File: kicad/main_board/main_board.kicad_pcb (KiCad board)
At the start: 4 copper layers, 0 parts

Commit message: board outline
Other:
- board outline added: 198.1 x 61 mm

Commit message: layout front panel connectors
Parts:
- added C1: 330pF, Capacitor_SMD:C_0603_1608Metric, F.Cu at (-84.8, 68.6)
- added C10: 10uF, Capacitor_SMD:C_0805_2012Metric, F.Cu at (-69.3, 107.0)
- added C11: 1.8nF, Capacitor_SMD:C_0603_1608Metric, F.Cu at (-84.8, 88.7)
- added C12: 10uF, Capacitor_SMD:C_0805_2012Metric, F.Cu at (-69.3, 110.0)
- added C13: 680pF, Capacitor_SMD:C_0603_1608Metric, F.Cu at (-84.8, 91.2)
- added C14: 10uF, Capacitor_SMD:C_0805_2012Metric, F.Cu at (-69.3, 113.0)
- added C15: 15pF, Capacitor_SMD:C_0603_1608Metric, F.Cu at (-84.8, 93.7)
- added C16: 10uF, Capacitor_SMD:C_0805_2012Metric, F.Cu at (-69.3, 116.0)
- added C17: 33nF, Capacitor_SMD:C_0603_1608Metric, F.Cu at (-84.8, 96.2)
- added C18: 10uF, Capacitor_SMD:C_0805_2012Metric, F.Cu at (-69.3, 119.0)
- added C19: 10uF, Capacitor_SMD:C_0805_2012Metric, F.Cu at (-69.3, 122.1)
- added C2: 330pF, Capacitor_SMD:C_0603_1608Metric, F.Cu at (-84.8, 71.1)
- added C20: 33nF, Capacitor_SMD:C_0603_1608Metric, F.Cu at (-84.8, 98.7)
- added C21: 1uF, Capacitor_SMD:C_0603_1608Metric, F.Cu at (-84.8, 101.2)
- added C22: 10uF, Capacitor_SMD:C_0805_2012Metric, F.Cu at (-64.9, 104.0)
- added C23: 100nF, Capacitor_SMD:C_0603_1608Metric, F.Cu at (-80.8, 68.6)
- added C24: 1uF, Capacitor_SMD:C_0603_1608Metric, F.Cu at (-80.8, 71.1)
- added C25: 150pF, Capacitor_SMD:C_0603_1608Metric, F.Cu at (-80.8, 73.6)
- added C26: 47nF, Capacitor_SMD:C_0603_1608Metric, F.Cu at (-80.8, 76.1)
- added C27: 47nF, Capacitor_SMD:C_0603_1608Metric, F.Cu at (-80.8, 78.7)
- added C28: 150pF, Capacitor_SMD:C_0603_1608Metric, F.Cu at (-80.8, 81.2)
- added C29: 2.2uF, Capacitor_SMD:C_0603_1608Metric, F.Cu at (-80.8, 83.7)
- added C3: 10uF, Capacitor_SMD:C_0603_1608Metric, F.Cu at (-84.8, 73.6)
- added C30: 10uF, Capacitor_SMD:C_0805_2012Metric, F.Cu at (-64.9, 107.0)
- added C31: 100pF, Capacitor_SMD:C_0603_1608Metric, F.Cu at (-80.8, 86.2)
- added C32: 10uF, Capacitor_SMD:C_0805_2012Metric, F.Cu at (-64.9, 110.0)
- added C33: 1uF, Capacitor_SMD:C_0603_1608Metric, F.Cu at (-80.8, 88.7)
- added C34: 10uF, Capacitor_SMD:C_0805_2012Metric, F.Cu at (-64.9, 113.0)
- added C35: 10uF, Capacitor_SMD:C_0805_2012Metric, F.Cu at (-64.9, 116.0)
- added C36: 100nF, Capacitor_SMD:C_0603_1608Metric, F.Cu at (-80.8, 91.2)
- added C37: 10uF, Capacitor_SMD:C_0805_2012Metric, F.Cu at (-64.9, 119.0)
- added C38: 10uF, Capacitor_SMD:C_0805_2012Metric, F.Cu at (-64.9, 122.1)
- added C39: 10uF, Capacitor_SMD:C_0805_2012Metric, F.Cu at (-60.4, 104.0)
- added C4: 1uF, Capacitor_SMD:C_0603_1608Metric, F.Cu at (-84.8, 76.1)
- added C40: 10uF, Capacitor_SMD:C_0805_2012Metric, F.Cu at (-60.4, 107.0)
- added C41: 10uF, Capacitor_SMD:C_0805_2012Metric, F.Cu at (-60.4, 110.0)
- added C42: 100nF, Capacitor_SMD:C_0603_1608Metric, F.Cu at (-80.8, 93.7)
- added C43: 10uF, Capacitor_SMD:C_0805_2012Metric, F.Cu at (-60.4, 113.0)
- added C44: 10uF, Capacitor_SMD:C_0805_2012Metric, F.Cu at (-60.4, 116.0)
- added C45: 100nF, Capacitor_SMD:C_0603_1608Metric, F.Cu at (-80.8, 96.2)
- added C46: 100nF, Capacitor_SMD:C_0603_1608Metric, F.Cu at (-80.8, 98.7)
- added C47: 100nF, Capacitor_SMD:C_0603_1608Metric, F.Cu at (-80.8, 101.2)
- added C48: 100nF, Capacitor_SMD:C_0603_1608Metric, F.Cu at (-76.8, 68.6)
- added C49: 22uF, Capacitor_SMD:C_0805_2012Metric, F.Cu at (-60.4, 119.0)
- added C5: 100nF, Capacitor_SMD:C_0603_1608Metric, F.Cu at (-84.8, 78.7)
- added C50: 22uF, Capacitor_SMD:C_0805_2012Metric, F.Cu at (-60.4, 122.1)
- added C51: 10uF, Capacitor_SMD:C_0603_1608Metric, F.Cu at (-76.8, 71.1)
- added C52: 100nF, Capacitor_SMD:C_0603_1608Metric, F.Cu at (-76.8, 73.6)
- added C53: 1uF, Capacitor_SMD:C_0603_1608Metric, F.Cu at (-76.8, 76.1)
- added C54: 100nF, Capacitor_SMD:C_0402_1005Metric, F.Cu at (-51.6, 103.5)
- added C55: 100nF, Capacitor_SMD:C_0402_1005Metric, F.Cu at (-51.6, 105.5)
- added C56: 100nF, Capacitor_SMD:C_0402_1005Metric, F.Cu at (-51.6, 107.4)
- added C57: 100nF, Capacitor_SMD:C_0402_1005Metric, F.Cu at (-51.6, 109.4)
- added C58: 100nF, Capacitor_SMD:C_0402_1005Metric, F.Cu at (-51.6, 111.4)
- added C59: 100nF, Capacitor_SMD:C_0402_1005Metric, F.Cu at (-51.6, 113.3)
- added C6: 10uF, Capacitor_SMD:C_0603_1608Metric, F.Cu at (-84.8, 81.2)
- added C60: 100nF, Capacitor_SMD:C_0402_1005Metric, F.Cu at (-51.6, 115.3)
- added C61: 100nF, Capacitor_SMD:C_0402_1005Metric, F.Cu at (-51.6, 117.3)
- added C62: 10uF, Capacitor_SMD:C_0603_1608Metric, F.Cu at (-76.8, 78.7)
- added C63: 1uF, Capacitor_SMD:C_0603_1608Metric, F.Cu at (-76.8, 81.2)
- added C64: 100nF, Capacitor_SMD:C_0603_1608Metric, F.Cu at (-76.8, 83.7)
- added C65: 15pF, Capacitor_SMD:C_0603_1608Metric, F.Cu at (-76.8, 86.2)
- added C66: 15pF, Capacitor_SMD:C_0603_1608Metric, F.Cu at (-76.8, 88.7)
- added C67: 100nF, Capacitor_SMD:C_0603_1608Metric, F.Cu at (-76.8, 91.2)
- added C68: 1uF, Capacitor_SMD:C_0603_1608Metric, F.Cu at (-76.8, 93.7)
- added C69: 1uF, Capacitor_SMD:C_0603_1608Metric, F.Cu at (-76.8, 96.2)
- added C7: 10uF, Capacitor_SMD:C_0805_2012Metric, F.Cu at (-69.3, 104.0)
- added C70: 100nF, Capacitor_SMD:C_0603_1608Metric, F.Cu at (-76.8, 98.7)
- added C71: 100nF, Capacitor_SMD:C_0603_1608Metric, F.Cu at (-76.8, 101.2)
- added C72: 1uF, Capacitor_SMD:C_0603_1608Metric, F.Cu at (-72.8, 68.6)
- added C73: 10uF, Capacitor_SMD:C_0603_1608Metric, F.Cu at (-72.8, 71.1)
- added C74: 10nF, Capacitor_SMD:C_0603_1608Metric, F.Cu at (-72.8, 73.6)
- added C75: 10nF, Capacitor_SMD:C_0603_1608Metric, F.Cu at (-72.8, 76.1)
- added C76: 10nF, Capacitor_SMD:C_0603_1608Metric, F.Cu at (-72.8, 78.7)
- added C77: 1uF, Capacitor_SMD:C_0603_1608Metric, F.Cu at (-72.8, 81.2)
- added C78: 100nF, Capacitor_SMD:C_0603_1608Metric, F.Cu at (-72.8, 83.7)
- added C79: 100nF, Capacitor_SMD:C_0603_1608Metric, F.Cu at (-72.8, 86.2)
- added C8: 33pF, Capacitor_SMD:C_0603_1608Metric, F.Cu at (-84.8, 83.7)
- added C80: 10uF, Capacitor_SMD:C_0603_1608Metric, F.Cu at (-72.8, 88.7)
- added C81: 1uF, Capacitor_SMD:C_0603_1608Metric, F.Cu at (-72.8, 91.2)
- added C82: 10uF, Capacitor_SMD:C_0603_1608Metric, F.Cu at (-72.8, 93.7)
- added C83: 10uF, Capacitor_SMD:C_0603_1608Metric, F.Cu at (-72.8, 96.2)
- added C84: 100nF, Capacitor_SMD:C_0603_1608Metric, F.Cu at (-72.8, 98.7)
- added C85: 1uF, Capacitor_SMD:C_0603_1608Metric, F.Cu at (-72.8, 101.2)
- added C9: 100pF, Capacitor_SMD:C_0603_1608Metric, F.Cu at (-84.8, 86.2)
- added D10: BAV99, Package_TO_SOT_SMD:SOT-23, F.Cu at (-44.3, 79.0)
- added D2: 3V3, Diode_SMD:D_SOD-323, F.Cu at (-40.3, 104.0)
- added D3: 30V, Diode_SMD:D_SOD-323, F.Cu at (-40.3, 106.9)
- added D4: 30V, Diode_SMD:D_SOD-323, F.Cu at (-40.3, 109.9)
- added D5: 30V, Diode_SMD:D_SOD-323, F.Cu at (-40.3, 112.8)
- added D6: 30V, Diode_SMD:D_SOD-323, F.Cu at (-40.3, 115.8)
- added D7: PWR, LED_SMD:LED_0603_1608Metric, F.Cu at (-39.8, 97.8)
- added D8: BAV99, Package_TO_SOT_SMD:SOT-23, F.Cu at (-44.3, 69.8)
- added D9: BAV99, Package_TO_SOT_SMD:SOT-23, F.Cu at (-44.3, 74.4)
- added FID1: Fiducial, Fiducial:Fiducial_1mm_Mask2mm, F.Cu at (-14.0, 36.1)
- added FID2: Fiducial, Fiducial:Fiducial_1mm_Mask2mm, F.Cu at (-14.0, 39.6)
- added FID3: Fiducial, Fiducial:Fiducial_1mm_Mask2mm, F.Cu at (-14.0, 43.2)
- added H1: MountingHole, MountingHole:MountingHole_2.2mm_M2, F.Cu at (53.3, 68.6)
- added H2: MountingHole, MountingHole:MountingHole_2.2mm_M2, F.Cu at (246.4, 68.6)
- added H3: MountingHole, MountingHole:MountingHole_2.2mm_M2, F.Cu at (246.4, 124.5)
- added H4: MountingHole, MountingHole:MountingHole_2.2mm_M2, F.Cu at (53.3, 124.5)
- added H5: MountingHole, MountingHole:MountingHole_2.2mm_M2, F.Cu at (-27.9, 39.4)
- added J1: USB_C, Connector_USB:USB_C_Receptacle_GCT_USB4105-xx-A_16P_TopMnt_Horizontal, F.Cu at (88.9, 124.6)
- added J10: LINE_ALT, Connector_PinHeader_2.54mm:PinHeader_1x04_P2.54mm_Vertical, F.Cu at (133.3, 111.8)
- added J11: LINE, SaawLib:PJ-3062-CO, F.Cu at (129.5, 127.0)
- added J12: DRV1, Connector_PinSocket_2.54mm:PinSocket_1x13_P2.54mm_Vertical, F.Cu at (-59.7, 148.6)
- added J13: DRV2, Connector_PinSocket_2.54mm:PinSocket_1x13_P2.54mm_Vertical, F.Cu at (-12.7, 146.1)
- added J14: CH_IN, Connector_PinSocket_2.54mm:PinSocket_1x13_P2.54mm_Vertical, F.Cu at (-51.6, 148.6)
- added J15: CH1, SaawLib:PJ-3062-CO, F.Cu at (182.9, 127.0)
- added J16: CH2, SaawLib:PJ-3062-CO, F.Cu at (200.7, 127.0)
- added J17: CH3, SaawLib:PJ-3062-CO, F.Cu at (218.4, 127.0)
- added J18: CH4, SaawLib:PJ-3062-CO, F.Cu at (236.2, 127.0)
- added J2: TRIG_A, SaawLib:PJ-3062-CO, F.Cu at (147.3, 127.0)
- added J3: TRIG_B, SaawLib:PJ-3062-CO, F.Cu at (162.6, 127.0)
- added J4: BAT, Connector_AMASS:AMASS_XT30UPB-M_1x02_P5.0mm_Vertical, F.Cu at (-22.9, 163.8)
- added J5: BAT_LINK, Connector_JST:JST_XH_B4B-XH-A_1x04_P2.50mm_Vertical, F.Cu at (-6.41, 159.3)
- added J6: FRONT_PANEL, Connector_JST:JST_XH_B8B-XH-A_1x08_P2.50mm_Vertical, F.Cu at (-45.8, 154.2)
- added J7: I2C, Connector_PinHeader_2.54mm:PinHeader_1x04_P2.54mm_Vertical, F.Cu at (-47.0, 168.8)
- added J8: SWD, Connector_PinHeader_2.54mm:PinHeader_1x03_P2.54mm_Vertical, F.Cu at (-31.8, 171.5)
- added J9: MIC, SaawLib:PJ-3062-CO, F.Cu at (114.3, 127.0)
- added JP1: BAT_4S, Jumper:SolderJumper-2_P1.3mm_Bridged_RoundedPad1.0x1.5mm, F.Cu at (-34.3, 94.4)
- added JP2: LED, Jumper:SolderJumper-2_P1.3mm_Bridged_RoundedPad1.0x1.5mm, F.Cu at (-34.3, 98.0)
- added JP3: BOOT, Connector_PinHeader_2.54mm:PinHeader_1x02_P2.54mm_Vertical, F.Cu at (-19.1, 174.0)
- added JP4: CT1, Connector_PinHeader_2.54mm:PinHeader_1x02_P2.54mm_Vertical, F.Cu at (191.8, 115.6)
- added JP5: CT2, Connector_PinHeader_2.54mm:PinHeader_1x02_P2.54mm_Vertical, F.Cu at (209.6, 115.6)
- added JP6: CT3, Connector_PinHeader_2.54mm:PinHeader_1x02_P2.54mm_Vertical, F.Cu at (227.3, 115.6)
- added JP7: CT4, Connector_PinHeader_2.54mm:PinHeader_1x02_P2.54mm_Vertical, F.Cu at (245.1, 115.6)
- added L1: 2.2uH, Inductor_SMD:L_Vishay_IHLP-2525, F.Cu at (-31.6, 88.7)
- added L2: 12uH, Inductor_SMD:L_Sunlord_SWPA6020S, F.Cu at (-46.3, 106.3)
- added L3: 12uH, Inductor_SMD:L_Sunlord_SWPA6020S, F.Cu at (-46.3, 114.0)
- added MK1: MIC, Sensor_Audio:CUI_CMC-4013-SMT, F.Cu at (-47.4, 120.5)
- added Q1: DMP3018SFV, Package_SON:Diodes_PowerDI3333-8, F.Cu at (-35.4, 118.8)
- added Q10: AO3401A, Package_TO_SOT_SMD:SOT-23, F.Cu at (-44.3, 92.9)
- added Q2: AO3400A, Package_TO_SOT_SMD:SOT-23, F.Cu at (-44.3, 83.6)
- added Q3: CSD17551Q3A, Package_SON:VSON-8_3.3x3.3mm_P0.65mm_NexFET, F.Cu at (-39.0, 69.9)
- added Q4: CSD17551Q3A, Package_SON:VSON-8_3.3x3.3mm_P0.65mm_NexFET, F.Cu at (-39.0, 74.8)
- added Q5: CSD17551Q3A, Package_SON:VSON-8_3.3x3.3mm_P0.65mm_NexFET, F.Cu at (-39.0, 79.8)
- added Q6: CSD17551Q3A, Package_SON:VSON-8_3.3x3.3mm_P0.65mm_NexFET, F.Cu at (-39.0, 84.7)
- added Q7: CSD25402Q3A, Package_SON:VSON-8_3.3x3.3mm_P0.65mm_NexFET, F.Cu at (-39.0, 89.7)
- added Q8: AO3400A, Package_TO_SOT_SMD:SOT-23, F.Cu at (-44.3, 88.3)
- added Q9: DMP3018SFV, Package_SON:Diodes_PowerDI3333-8, F.Cu at (-35.4, 123.7)
- added R1: 10k, Resistor_SMD:R_0603_1608Metric, F.Cu at (-68.8, 68.6)
- added R10: 100k, Resistor_SMD:R_0603_1608Metric, F.Cu at (-68.8, 91.2)
- added R11: 10k, Resistor_SMD:R_0603_1608Metric, F.Cu at (-68.8, 93.7)
- added R12: 22k, Resistor_SMD:R_0603_1608Metric, F.Cu at (-68.8, 96.2)
- added R13: 100, Resistor_SMD:R_1206_3216Metric, F.Cu at (-27.9, 104.1)
- added R14: 100k, Resistor_SMD:R_0603_1608Metric, F.Cu at (-68.8, 98.7)
- added R15: 22k, Resistor_SMD:R_0603_1608Metric, F.Cu at (-68.8, 101.2)
- added R16: 100k, Resistor_SMD:R_0603_1608Metric, F.Cu at (-64.8, 68.6)
- added R17: 2k, Resistor_SMD:R_1206_3216Metric, F.Cu at (-27.9, 107.4)
- added R18: 39k, Resistor_SMD:R_0603_1608Metric, F.Cu at (-64.8, 71.1)
- added R19: 300k, Resistor_SMD:R_0603_1608Metric, F.Cu at (-64.8, 73.6)
- added R2: 10k, Resistor_SMD:R_0603_1608Metric, F.Cu at (-68.8, 71.1)
- added R20: 220k, Resistor_SMD:R_0603_1608Metric, F.Cu at (-64.8, 76.1)
- added R21: 10k, Resistor_SMD:R_0603_1608Metric, F.Cu at (-64.8, 78.7)
- added R22: 4.99, Resistor_SMD:R_0603_1608Metric, F.Cu at (-64.8, 81.2)
- added R23: 0.01, Resistor_SMD:R_1206_3216Metric, F.Cu at (-27.9, 110.7)
- added R24: 10, Resistor_SMD:R_0603_1608Metric, F.Cu at (-64.8, 83.7)
- added R25: 4.99, Resistor_SMD:R_0603_1608Metric, F.Cu at (-64.8, 86.2)
- added R26: 10, Resistor_SMD:R_0603_1608Metric, F.Cu at (-64.8, 88.7)
- added R27: 10k, Resistor_SMD:R_0603_1608Metric, F.Cu at (-64.8, 91.2)
- added R28: 10k, Resistor_SMD:R_0603_1608Metric, F.Cu at (-64.8, 93.7)
- added R29: 27k, Resistor_SMD:R_0603_1608Metric, F.Cu at (-64.8, 96.2)
- added R3: 10k, Resistor_SMD:R_0603_1608Metric, F.Cu at (-68.8, 73.6)
- added R30: 10, Resistor_SMD:R_0603_1608Metric, F.Cu at (-64.8, 98.7)
- added R31: 0.01, Resistor_SMD:R_1206_3216Metric, F.Cu at (-27.9, 114.0)
- added R32: 10, Resistor_SMD:R_0603_1608Metric, F.Cu at (-64.8, 101.2)
- added R33: 39k, Resistor_SMD:R_0603_1608Metric, F.Cu at (-60.8, 68.6)
- added R34: 39k, Resistor_SMD:R_0603_1608Metric, F.Cu at (-60.8, 71.1)
- added R35: 100k, Resistor_SMD:R_0603_1608Metric, F.Cu at (-60.8, 73.6)
- added R36: 100k, Resistor_SMD:R_0603_1608Metric, F.Cu at (-60.8, 76.1)
- added R37: 1k, Resistor_SMD:R_0603_1608Metric, F.Cu at (-60.8, 78.7)
- added R38: 1M, Resistor_SMD:R_0603_1608Metric, F.Cu at (-60.8, 81.2)
- added R39: 100k, Resistor_SMD:R_0603_1608Metric, F.Cu at (-60.8, 83.7)
- added R4: 10k, Resistor_SMD:R_0603_1608Metric, F.Cu at (-68.8, 76.1)
- added R40: 2.2k, Resistor_SMD:R_0603_1608Metric, F.Cu at (-60.8, 86.2)
- added R41: 82k, Resistor_SMD:R_0603_1608Metric, F.Cu at (-60.8, 88.7)
- added R42: 22k, Resistor_SMD:R_0603_1608Metric, F.Cu at (-60.8, 91.2)
- added R43: 51k, Resistor_SMD:R_0603_1608Metric, F.Cu at (-60.8, 93.7)
- added R44: 22k, Resistor_SMD:R_0603_1608Metric, F.Cu at (-60.8, 96.2)
- added R45: 2.2k, Resistor_SMD:R_0603_1608Metric, F.Cu at (-60.8, 98.7)
- added R46: 10k, Resistor_SMD:R_0603_1608Metric, F.Cu at (-60.8, 101.2)
- added R47: 2.2k, Resistor_SMD:R_0603_1608Metric, F.Cu at (-56.7, 68.6)
- added R48: 27, Resistor_SMD:R_0603_1608Metric, F.Cu at (-56.7, 71.1)
- added R49: 27, Resistor_SMD:R_0603_1608Metric, F.Cu at (-56.7, 73.6)
- added R5: 100k, Resistor_SMD:R_0603_1608Metric, F.Cu at (-68.8, 78.7)
- added R50: 100k, Resistor_SMD:R_0603_1608Metric, F.Cu at (-56.7, 76.1)
- added R51: 2.2k, Resistor_SMD:R_0603_1608Metric, F.Cu at (-56.7, 78.7)
- added R52: 2.2k, Resistor_SMD:R_0603_1608Metric, F.Cu at (-56.7, 81.2)
- added R53: 100, Resistor_SMD:R_0603_1608Metric, F.Cu at (-56.7, 83.7)
- added R54: 1k, Resistor_SMD:R_0603_1608Metric, F.Cu at (-56.7, 86.2)
- added R55: 1k, Resistor_SMD:R_0603_1608Metric, F.Cu at (-56.7, 88.7)
- added R56: 10k, Resistor_SMD:R_0603_1608Metric, F.Cu at (-56.7, 91.2)
- added R57: 100k, Resistor_SMD:R_0603_1608Metric, F.Cu at (-56.7, 93.7)
- added R58: 100, Resistor_SMD:R_0603_1608Metric, F.Cu at (-56.7, 96.2)
- added R59: 2.2k, Resistor_SMD:R_0603_1608Metric, F.Cu at (-56.7, 98.7)
- added R6: 1k, Resistor_SMD:R_0603_1608Metric, F.Cu at (-68.8, 81.2)
- added R60: 100k, Resistor_SMD:R_0603_1608Metric, F.Cu at (-56.7, 101.2)
- added R61: 100k, Resistor_SMD:R_0603_1608Metric, F.Cu at (-52.7, 68.6)
- added R62: 1M, Resistor_SMD:R_0603_1608Metric, F.Cu at (-52.7, 71.1)
- added R63: 1k, Resistor_SMD:R_0603_1608Metric, F.Cu at (-52.7, 73.6)
- added R64: 2.2k, Resistor_SMD:R_0603_1608Metric, F.Cu at (-52.7, 76.1)
- added R65: 1k, Resistor_SMD:R_0603_1608Metric, F.Cu at (-52.7, 78.7)
- added R66: 1k, Resistor_SMD:R_0603_1608Metric, F.Cu at (-52.7, 81.2)
- added R67: 1k, Resistor_SMD:R_0603_1608Metric, F.Cu at (-52.7, 83.7)
- added R68: 1k, Resistor_SMD:R_0603_1608Metric, F.Cu at (-52.7, 86.2)
- added R69: 100k, Resistor_SMD:R_0603_1608Metric, F.Cu at (-52.7, 88.7)
- added R7: 1k, Resistor_SMD:R_0603_1608Metric, F.Cu at (-68.8, 83.7)
- added R70: 100k, Resistor_SMD:R_0603_1608Metric, F.Cu at (-52.7, 91.2)
- added R71: 10k, Resistor_SMD:R_0603_1608Metric, F.Cu at (-52.7, 93.7)
- added R72: 1M, Resistor_SMD:R_0603_1608Metric, F.Cu at (-52.7, 96.2)
- added R73: 1M, Resistor_SMD:R_0603_1608Metric, F.Cu at (-52.7, 98.7)
- added R74: 100k, Resistor_SMD:R_0603_1608Metric, F.Cu at (-52.7, 101.2)
- added R75: 100k, Resistor_SMD:R_0603_1608Metric, F.Cu at (-48.7, 68.6)
- added R76: 1k, Resistor_SMD:R_0603_1608Metric, F.Cu at (-48.7, 71.1)
- added R77: 1k, Resistor_SMD:R_0603_1608Metric, F.Cu at (-48.7, 73.6)
- added R78: 2.2k, Resistor_SMD:R_0603_1608Metric, F.Cu at (-48.7, 76.1)
- added R79: 2.2k, Resistor_SMD:R_0603_1608Metric, F.Cu at (-48.7, 78.7)
- added R8: 1k, Resistor_SMD:R_0603_1608Metric, F.Cu at (-68.8, 86.2)
- added R80: 10k, Resistor_SMD:R_0603_1608Metric, F.Cu at (-48.7, 81.2)
- added R81: 10k, Resistor_SMD:R_0603_1608Metric, F.Cu at (-48.7, 83.7)
- added R82: 1M, Resistor_SMD:R_0603_1608Metric, F.Cu at (-48.7, 86.2)
- added R83: 6.2k, Resistor_SMD:R_0603_1608Metric, F.Cu at (-48.7, 88.7)
- added R84: 82k, Resistor_SMD:R_0603_1608Metric, F.Cu at (-48.7, 91.2)
- added R85: 1.2k, Resistor_SMD:R_0603_1608Metric, F.Cu at (-48.7, 93.7)
- added R86: 100k, Resistor_SMD:R_0603_1608Metric, F.Cu at (-48.7, 96.2)
- added R87: 10k, Resistor_SMD:R_0603_1608Metric, F.Cu at (-48.7, 98.7)
- added R9: 1k, Resistor_SMD:R_0603_1608Metric, F.Cu at (-68.8, 88.7)
- added SW1: PWR, Button_Switch_THT:SW_Tactile_SPST_Angled_PTS645Vx31-2LFS, F.Cu at (65.8, 121.3)
- added TP1: GND, TestPoint:TestPoint_Pad_D1.0mm, F.Cu at (-85.3, 104.0)
- added TP10: CELL, TestPoint:TestPoint_Pad_D1.0mm, F.Cu at (-82.2, 110.1)
- added TP11: GND, TestPoint:TestPoint_Pad_D1.0mm, F.Cu at (-82.2, 113.2)
- added TP12: GND, TestPoint:TestPoint_Pad_D1.0mm, F.Cu at (-82.2, 116.2)
- added TP13: VIN, TestPoint:TestPoint_Pad_D1.0mm, F.Cu at (-82.2, 119.3)
- added TP14: GND, TestPoint:TestPoint_Pad_D1.0mm, F.Cu at (-82.2, 122.3)
- added TP15: GND, TestPoint:TestPoint_Pad_D1.0mm, F.Cu at (-79.2, 104.0)
- added TP16: GND, TestPoint:TestPoint_Pad_D1.0mm, F.Cu at (-79.2, 107.1)
- added TP17: GND, TestPoint:TestPoint_Pad_D1.0mm, F.Cu at (-79.2, 110.1)
- added TP18: VIN, TestPoint:TestPoint_Pad_D1.0mm, F.Cu at (-79.2, 113.2)
- added TP19: VIN, TestPoint:TestPoint_Pad_D1.0mm, F.Cu at (-79.2, 116.2)
- added TP2: GND, TestPoint:TestPoint_Pad_D1.0mm, F.Cu at (-85.3, 107.1)
- added TP20: 5V, TestPoint:TestPoint_Pad_D1.0mm, F.Cu at (-79.2, 119.3)
- added TP21: 3V3, TestPoint:TestPoint_Pad_D1.0mm, F.Cu at (-79.2, 122.3)
- added TP22: GND, TestPoint:TestPoint_Pad_D1.0mm, F.Cu at (-76.1, 104.0)
- added TP23: DSCL, TestPoint:TestPoint_Pad_D1.0mm, F.Cu at (-76.1, 107.1)
- added TP24: DSDA, TestPoint:TestPoint_Pad_D1.0mm, F.Cu at (-76.1, 110.1)
- added TP25: ~{LDAC}, TestPoint:TestPoint_Pad_D1.0mm, F.Cu at (-76.1, 113.2)
- added TP26: RDY, TestPoint:TestPoint_Pad_D1.0mm, F.Cu at (-76.1, 116.2)
- added TP27: GND, TestPoint:TestPoint_Pad_D1.0mm, F.Cu at (-76.1, 119.3)
- added TP28: RUN, TestPoint:TestPoint_Pad_D1.0mm, F.Cu at (-76.1, 122.3)
- added TP29: VREF, TestPoint:TestPoint_Pad_D1.0mm, F.Cu at (-73.1, 104.0)
- added TP3: SBU1, TestPoint:TestPoint_Pad_D1.0mm, F.Cu at (-85.3, 110.1)
- added TP30: GND, TestPoint:TestPoint_Pad_D1.0mm, F.Cu at (-73.1, 107.1)
- added TP31: MOP, TestPoint:TestPoint_Pad_D1.0mm, F.Cu at (-73.1, 110.1)
- added TP32: ROP, TestPoint:TestPoint_Pad_D1.0mm, F.Cu at (-73.1, 113.2)
- added TP33: TOP, TestPoint:TestPoint_Pad_D1.0mm, F.Cu at (-73.1, 116.2)
- added TP34: GND, TestPoint:TestPoint_Pad_D1.0mm, F.Cu at (-73.1, 119.3)
- added TP4: SBU2, TestPoint:TestPoint_Pad_D1.0mm, F.Cu at (-85.3, 113.2)
- added TP5: VBUS, TestPoint:TestPoint_Pad_D1.0mm, F.Cu at (-85.3, 116.2)
- added TP6: ILIM, TestPoint:TestPoint_Pad_D1.0mm, F.Cu at (-85.3, 119.3)
- added TP7: CHRG_OK, TestPoint:TestPoint_Pad_D1.0mm, F.Cu at (-85.3, 122.3)
- added TP8: ~{PROCHOT}, TestPoint:TestPoint_Pad_D1.0mm, F.Cu at (-82.2, 104.0)
- added TP9: VSYS, TestPoint:TestPoint_Pad_D1.0mm, F.Cu at (-82.2, 107.1)
- added U1: SRV05-4, Package_TO_SOT_SMD:SOT-23-6, F.Cu at (-55.6, 104.9)
- added U10: MCP4451-503, Package_SO:TSSOP-20_4.4x6.5mm_P0.65mm, F.Cu at (-31.8, 80.7)
- added U11: MCP6002, Package_SO:MSOP-8_3x3mm_P0.65mm, F.Cu at (-34.5, 109.4)
- added U12: MCP6002, Package_SO:MSOP-8_3x3mm_P0.65mm, F.Cu at (-34.5, 114.0)
- added U2: SRV05-4, Package_TO_SOT_SMD:SOT-23-6, F.Cu at (-55.6, 109.5)
- added U3: FUSB302B, Package_DFN_QFN:WQFN-14-1EP_2.5x2.5mm_P0.5mm_EP1.45x1.45mm, F.Cu at (-55.8, 123.4)
- added U4: BQ25703A, Package_DFN_QFN:Texas_S-PWQFN-N32_EP2.8x2.8mm_ThermalVias, F.Cu at (-29.0, 95.8)
- added U5: TPS560430, Package_TO_SOT_SMD:SOT-23-6, F.Cu at (-55.6, 114.1)
- added U6: TPS560430, Package_TO_SOT_SMD:SOT-23-6, F.Cu at (-55.6, 118.8)
- added U7: MCP4728, Package_SO:MSOP-10_3x3mm_P0.5mm, F.Cu at (-34.5, 104.8)
- added U8: RP2040, Package_DFN_QFN:QFN-56-1EP_7x7mm_P0.4mm_EP3.2x3.2mm, F.Cu at (-31.9, 72.0)
- added U9: W25Q128JVP, Package_SON:WSON-8-1EP_6x5mm_P1.27mm_EP3.4x4.3mm, F.Cu at (-28.5, 119.6)
- added Y1: 12MHz, Crystal:Crystal_SMD_3225-4Pin_3.2x2.5mm, F.Cu at (-39.2, 94.3)
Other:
- board text added: "Button Cap"
- board text added: "Front Panel ->"

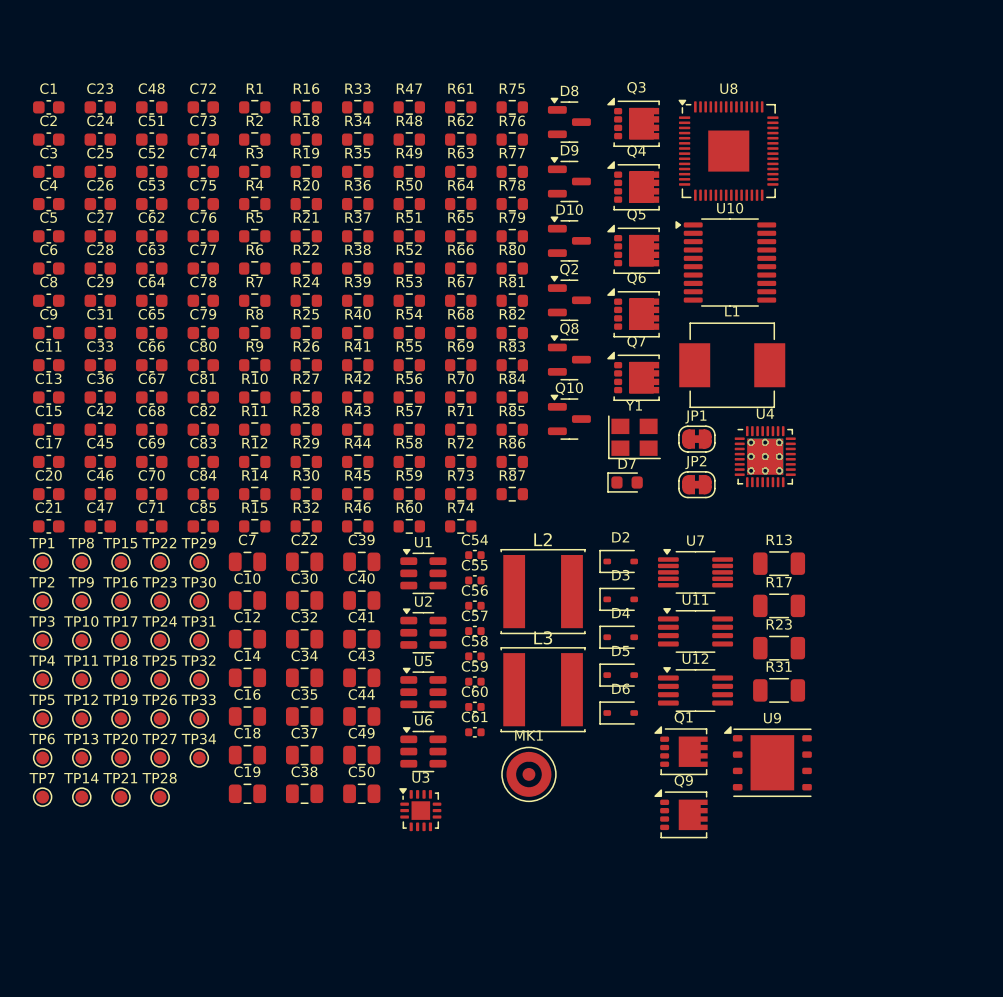
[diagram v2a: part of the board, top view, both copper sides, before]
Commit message: add VBUS tvs
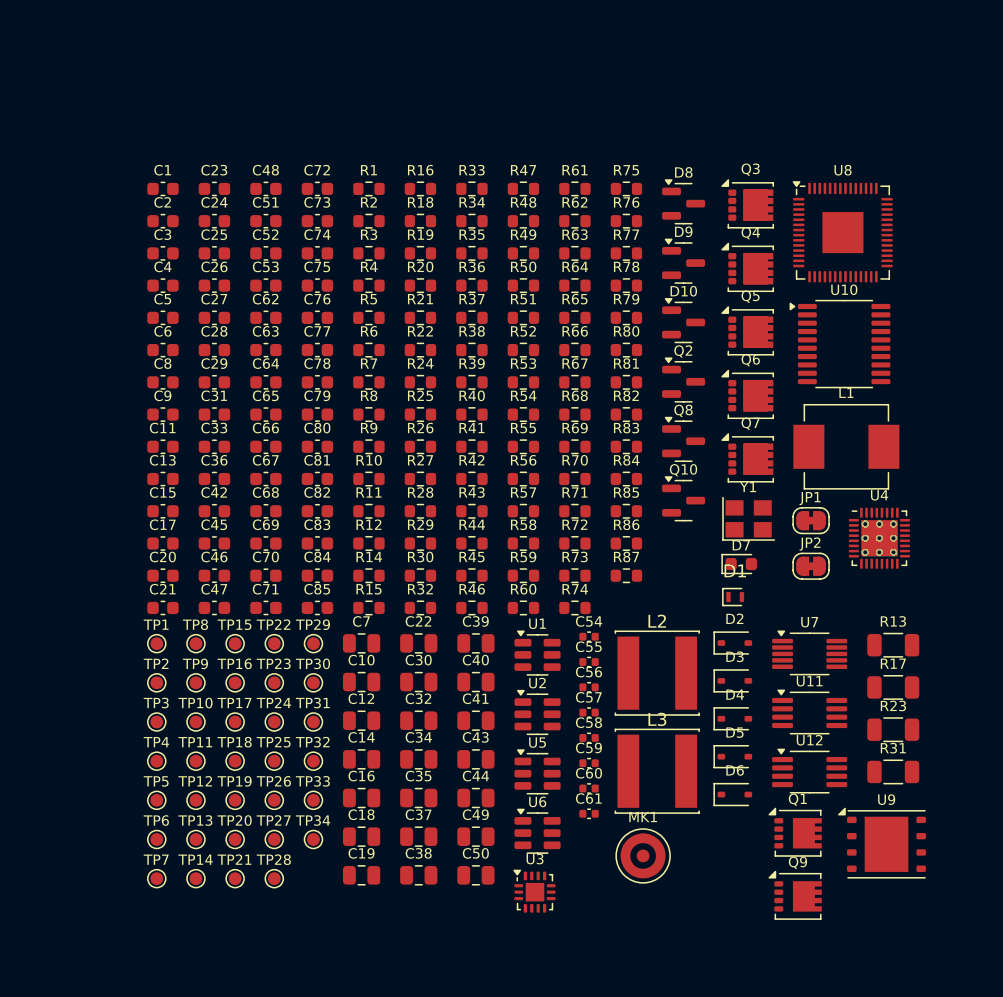
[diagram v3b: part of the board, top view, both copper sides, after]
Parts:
- added D1: 22V, Diode_SMD:ST_QFN-2L_1.6x1.0mm, F.Cu at (-31.4, 106.7)
- moved R19 10.9 mm to (-55.9, 80.0)
- moved R22 10.9 mm to (-55.9, 87.5)
- moved R26 10.9 mm to (-55.9, 95.0)
- moved R28 10.9 mm to (-55.9, 100.1)
- moved R32 10.9 mm to (-55.9, 107.6)
- moved JP1 10.9 mm to (-25.4, 100.8)
- moved JP2 10.9 mm to (-25.4, 104.3)
- moved U12 10.9 mm to (-25.6, 120.4)
- moved U7 10.9 mm to (-25.6, 111.2)
- moved Y1 10.9 mm to (-30.3, 100.7)
- moved C11 10.9 mm to (-75.9, 95.0)
- moved C12 10.9 mm to (-60.5, 116.4)
- moved C15 10.9 mm to (-75.9, 100.1)
- moved C18 10.9 mm to (-60.5, 125.4)
- moved C21 10.9 mm to (-75.9, 107.6)
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
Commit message: add mainboard pcb
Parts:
- removed the R27 at (-55.9, 97.5)
- removed the TP13 at (-73.3, 125.6)
- removed the TP2 at (-76.4, 113.4)
- removed the TP23 at (-67.2, 113.4)
- removed TP24: DSDA, TestPoint:TestPoint_Pad_D1.0mm
- removed TP30, TP34: GND, TestPoint:TestPoint_Pad_D1.0mm
- removed TP31: MOP, TestPoint:TestPoint_Pad_D1.0mm
- removed TP32: ROP, TestPoint:TestPoint_Pad_D1.0mm
- removed TP33: TOP, TestPoint:TestPoint_Pad_D1.0mm
- removed the TP7 at (-76.4, 128.7)
- removed the TP8 at (-73.3, 110.4)
- added H6: MountingHole, MountingHole:MountingHole_2.2mm_M2, F.Cu at (142.2, 111.8)
- added H7: MountingHole, MountingHole:MountingHole_2.2mm_M2, F.Cu at (221.0, 68.6)
- added H8: MountingHole, MountingHole:MountingHole_2.2mm_M2, F.Cu at (246.4, 111.8)
- added NT1: ~, NetTie:NetTie-2_SMD_Pad2.0mm, F.Cu at (180.6, 69.3)
- added NT2: ~, NetTie:NetTie-2_SMD_Pad2.0mm, F.Cu at (180.6, 67.4)
- added R87: 0.1, Resistor_SMD:R_2512_6332Metric, F.Cu at (181.9, 72.3)
- C65, C66: footprint Capacitor_SMD:C_0603_1608Metric -> Capacitor_SMD:C_0402_1005Metric
- J12: renamed from J13; value DRV2 -> DRV; footprint Connector_PinSocket_2.54mm:PinSocket_1x13_P2.54mm_Vertical -> Connector_PinSocket_2.54mm:PinSocket_2x08_P2.54mm_Vertical
- J13: renamed from J12; value DRV1 -> DRV_PWR; footprint Connector_PinSocket_2.54mm:PinSocket_1x13_P2.54mm_Vertical -> Connector_PinSocket_2.54mm:PinSocket_1x05_P2.54mm_Vertical
- J14: footprint Connector_PinSocket_2.54mm:PinSocket_1x13_P2.54mm_Vertical -> Connector_PinHeader_2.54mm:PinHeader_1x12_P2.54mm_Vertical
- J6: footprint Connector_JST:JST_XH_B8B-XH-A_1x08_P2.50mm_Vertical -> Connector_IDC:IDC-Header_2x04_P2.54mm_Vertical
- R52: renamed from R48; footprint Resistor_SMD:R_0603_1608Metric -> Resistor_SMD:R_0402_1005Metric
- R53: renamed from R49; footprint Resistor_SMD:R_0603_1608Metric -> Resistor_SMD:R_0402_1005Metric
- R59: renamed from R55; footprint Resistor_SMD:R_0603_1608Metric -> Resistor_SMD:R_0402_1005Metric
- TP1: moved to B.Cu
- TP2: renamed from TP3; moved to B.Cu
- TP3: renamed from TP4; moved to B.Cu
- U9: value W25Q128JVP -> W25Q128JVS; footprint Package_SON:WSON-8-1EP_6x5mm_P1.27mm_EP3.4x4.3mm -> Package_SO:SOIC-8_5.23x5.23mm_P1.27mm
- moved TP22 280.9 mm to (210.1, 84.2)
- moved C66 279.4 mm to (211.4, 88.9), turned to -90 degrees
- moved C65 279.4 mm to (211.5, 92.0), turned to 90 degrees
- moved FID3 268.3 mm to (246.4, 108.0)
- moved C62 263.5 mm to (195.6, 81.9), turned to 180 degrees
- moved FID1 263.0 mm to (246.4, 73.7)
- moved TP21 262.8 mm to (192.0, 82.5)
- moved C53 262.8 mm to (194.9, 85.3), turned to 180 degrees
- moved C63 262.8 mm to (194.9, 87.0), turned to 180 degrees
- moved TP23 262.8 mm to (197.4, 85.3), turned to 90 degrees
- moved J14 261.2 mm to (207.0, 111.8), turned to 90 degrees
- moved R59 256.3 mm to (208.4, 91.1), turned to 180 degrees
- moved R54 255.5 mm to (207.6, 83.3), turned to 90 degrees
- moved C61 253.6 mm to (208.4, 88.9)
- moved C64 253.1 mm to (185.2, 94.6), turned to -90 degrees
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- renumbered R85 to R18, R18 to R19, R84 to R20, R19 to R21, R20 to R22, R21 to R23, R22 to R24, R23 to R25, R24 to R26, R25 to R27, R26 to R28, R28 to R29, R29 to R30, R87 to R31, R86 to R32, R30 to R33, R31 to R34, R32 to R35, R33 to R36, R34 to R37, R35 to R38, R36 to R39, R37 to R40, R38 to R41, R39 to R42, R40 to R43, R41 to R44, R83 to R45, R42 to R46, R43 to R47, R44 to R48, R45 to R49, R46 to R50, R47 to R51, R50 to R54, R51 to R55, R52 to R56, R53 to R57, R54 to R58, R56 to R60, R57 to R61, R58 to R62, R59 to R63, R60 to R64, R61 to R65, R62 to R66, R63 to R67, R64 to R68, R65 to R69, R66 to R70, R67 to R71, R68 to R72, R69 to R73, R70 to R74, R71 to R75, R72 to R76, R73 to R77, R74 to R78, R75 to R79, R76 to R80, R77 to R81, R78 to R82, R79 to R83, R80 to R84, R81 to R85, R82 to R86, TP14 to TP10, TP15 to TP11, TP16 to TP12, TP17 to TP13, TP18 to TP14, TP19 to TP15, TP20 to TP16, TP21 to TP17, TP22 to TP18, TP25 to TP19, TP26 to TP20, TP27 to TP21, TP28 to TP22, TP29 to TP23, TP5 to TP4, TP6 to TP5, TP9 to TP6, TP10 to TP7, TP11 to TP8, TP12 to TP9
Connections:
- J12 pad 10: GND -> /Controller/CH3_GB
- J12 pad 11: /Controller/CH1_GB -> /Controller/CH2_LVL
- J12 pad 12: /Controller/CH1_GA -> /Controller/CH3_GA
- J12 pad 13: GND -> /Controller/CH1_LVL
- J12 pad 3: /Controller/CH4_GA -> +3.3V
- J12 pad 4: GND -> /Controller/CH4_GA
- J12 pad 5: /Controller/CH3_GB -> unconnected-(J12-Pin_5-Pad5)
- J12 pad 6: /Controller/CH3_GA -> /Controller/CH1_GB
- J12 pad 7: GND -> /Controller/CH4_LVL
- J12 pad 8: /Controller/CH2_GB -> /Controller/CH1_GA
- J12 pad 9: /Controller/CH2_GA -> /Controller/CH3_LVL
- J13 pad 1: VIN -> /Output/PGND
- J13 pad 2: VIN -> /Output/PGND
- J13 pad 4: GND -> VIN
- J13 pad 5: +3.3V -> VIN
- J14 pad 7: unconnected-(J14-Pin_7-Pad7) -> Net-(J14-Pin_7)
- J17 pad S: Net-(J14-Pin_8) -> Net-(J14-Pin_7)
- J17 pad T: Net-(J14-Pin_10) -> Net-(J14-Pin_9)
- J18 pad S: Net-(J14-Pin_11) -> Net-(J14-Pin_10)
- J18 pad T: Net-(J14-Pin_13) -> Net-(J14-Pin_12)
- J6 pad 1: +5V -> +3.3V
- J6 pad 2: +3.3V -> +5V
- J6 pad 4: /Controller/BCLK -> GND
- J6 pad 5: /Controller/WS -> /Controller/BCLK
- J6 pad 6: /Controller/TXD1 -> /Controller/WS
- J6 pad 8: GND -> /Controller/TXD1
- JP6 pad 1: Net-(J14-Pin_9) -> Net-(J14-Pin_8)
- JP7 pad 1: Net-(J14-Pin_12) -> Net-(J14-Pin_11)
- R28 pad 2: VCHRG -> VBUS
- U1 pad 1: /Input/USB_D+ -> /Input/USB_D-
- U1 pad 3: /Input/USB_D- -> /Input/USB_D+
- U1 pad 4: /Input/CC1 -> /Input/CC2
- U1 pad 6: /Input/CC2 -> /Input/CC1
- U4 pad 11: Net-(U4-~{PROCHOT}) -> unconnected-(U4-~{PROCHOT}-Pad11)
- U4 pad 4: /Charger/CHRG_OK -> unconnected-(U4-CHRG_OK-Pad4)
- U8 pad 11: /Controller/TXD1 -> /Controller/SDA_DAC
- U8 pad 12: /Controller/RXD1 -> /Controller/SCL_DAC
- U8 pad 13: /Controller/SDA_DAC -> /Controller/DRV_EN
- U8 pad 14: /Controller/SCL_DAC -> /Audio/~{PIP_EN}
- U8 pad 15: /Controller/PWR_CTRL -> /Controller/~{TRIG_B1}
- U8 pad 16: /Controller/~{INT_PD} -> /Controller/~{TRIG_B2}
- U8 pad 17: /Audio/~{PIP_EN} -> /Controller/~{TRIG_A1}
- U8 pad 18: /Controller/DIN -> /Controller/~{TRIG_A2}
- U8 pad 19: unconnected-(U8-TESTEN-Pad19) -> GND
- U8 pad 2: /Controller/CH1_GA -> /Controller/CH2_GA
- U8 pad 27: /Controller/BCLK -> /Controller/DIN
- U8 pad 29: /Controller/DRV_EN -> /Controller/BCLK
- U8 pad 3: /Controller/CH1_GB -> /Controller/CH2_GB
- U8 pad 30: /Controller/DISCH_EN -> /Controller/PWR_CTRL
- U8 pad 31: /Charger/SDA -> /Controller/TXD1
- U8 pad 32: /Charger/SCL -> /Controller/RXD1
- U8 pad 34: /Controller/~{TRIG_A1} -> /Charger/SDA
- U8 pad 35: /Controller/~{TRIG_A2} -> /Charger/SCL
- U8 pad 36: /Controller/~{TRIG_B1} -> /Controller/DISCH_EN
- U8 pad 37: /Controller/~{TRIG_B2} -> /Controller/~{INT_PD}
- U8 pad 39: /Audio/AUDIO_L -> /Audio/MIC
- U8 pad 4: /Controller/CH2_GA -> /Controller/CH3_GA
- U8 pad 41: /Audio/MIC -> /Audio/AUDIO_L
- U8 pad 5: /Controller/CH2_GB -> /Controller/CH3_GB
- U8 pad 6: /Controller/CH3_GA -> /Controller/CH1_GA
- U8 pad 7: /Controller/CH3_GB -> /Controller/CH1_GB
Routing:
- net /Charger/SCL: track 0.00 -> 199.0 mm, vias 0 -> 2
- net /Charger/SDA: track 0.00 -> 190.2 mm, vias 0 -> 2
- net /Input/USB_D-: track 0.00 -> 133.3 mm
- net /Controller/~{INT_PD}: track 0.00 -> 131.9 mm, vias 0 -> 2
- net /Input/USB_D+: track 0.00 -> 129.9 mm, vias 0 -> 2
- net /Controller/DISCH_EN: track 0.00 -> 129.2 mm, vias 0 -> 2
- net /Controller/PWR_CTRL: track 0.00 -> 121.8 mm, vias 0 -> 2
- net /Controller/SWC: track 0.00 -> 106.8 mm, vias 0 -> 2
- net /Audio/MIC: track 0.00 -> 106.3 mm, vias 0 -> 3
- net +3.3V: track 0.00 -> 104.9 mm, vias 0 -> 33
- net /Controller/SWD: track 0.00 -> 102.4 mm, vias 0 -> 2
- net /Audio/~{PIP_EN}: track 0.00 -> 97.9 mm, vias 0 -> 2
- net /Controller/DIN: track 0.00 -> 94.0 mm
- net /Controller/BCLK: track 0.00 -> 91.3 mm
- net /Audio/AUDIO_R: track 0.00 -> 89.9 mm, vias 0 -> 2
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- added copper zone on F.Cu, net +3.3V
- added copper zone on In2.Cu, net +3.3V
- added copper zone on F.Cu, net +5V
- added copper zone on F.Cu, net /Controller/DVDD
- added copper zone on F.Cu, net /Controller/SENSE
- added copper zone on B.Cu, net /Output/PGND
- added copper zone on F.Cu, net /Output/PGND
- added copper zone on In1.Cu, net /Output/PGND
- added copper zone on B.Cu, net GND
- added copper zone on F.Cu, net GND
- added copper zone on In1.Cu, net GND
- added copper zone on In2.Cu, net GND
- added copper zone on F.Cu, net Net-(C33-Pad1)
- added copper zone on F.Cu, net Net-(J4-Pin_2)
- added copper zone on F.Cu, net Net-(Q3-D)
- added copper zone on In2.Cu, net Net-(Q3-D)
- added copper zone on F.Cu, net Net-(Q4-D)
- added copper zone on In2.Cu, net Net-(Q4-D)
- added copper zone on F.Cu, net Net-(Q5-D)
- added copper zone on In2.Cu, net Net-(Q5-D)
- added copper zone on F.Cu, net Net-(U5-SW)
- added copper zone on F.Cu, net Net-(U6-SW)
- added copper zone on F.Cu, net VBUS
- added copper zone on In2.Cu, net VBUS
- added copper zone on F.Cu, net VCHRG
- added copper zone on In2.Cu, net VCHRG
- added copper zone on F.Cu, net VIN
- added copper zone on In2.Cu, net VIN
- added copper zone on F.Cu, net VSYS
- added copper zone on In2.Cu, net VSYS
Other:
- board text added: "JLCJLCJLCJLC"
- board text added: "SW32 ${PROJECTNAME} rev${REVISION} ${hash}"

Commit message: cleanup
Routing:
- net GND: vias 255 -> 267
